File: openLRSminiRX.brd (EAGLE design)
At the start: 21.3 x 21.8 mm, 33 parts, among them IC1 MCP1703CB, U1 ATMEGA328P, Y1 16MHz

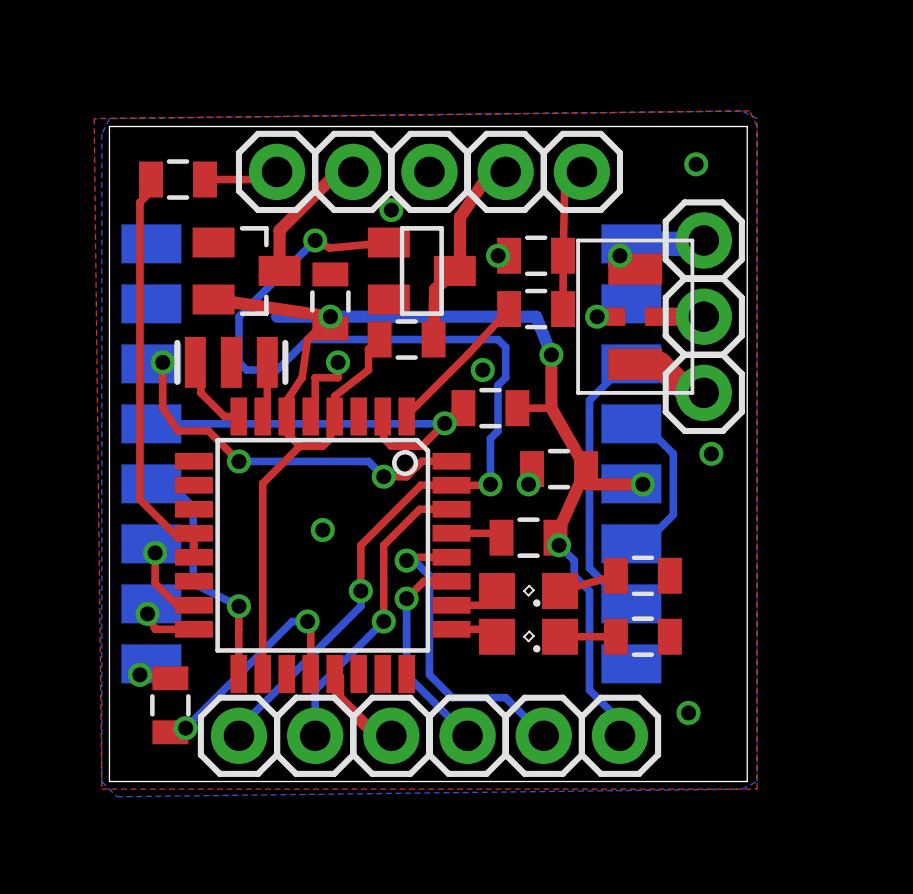
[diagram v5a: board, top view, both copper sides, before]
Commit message: Make filtter 'mandatory'. It is still possible to use without filter by soldering to pad directly.
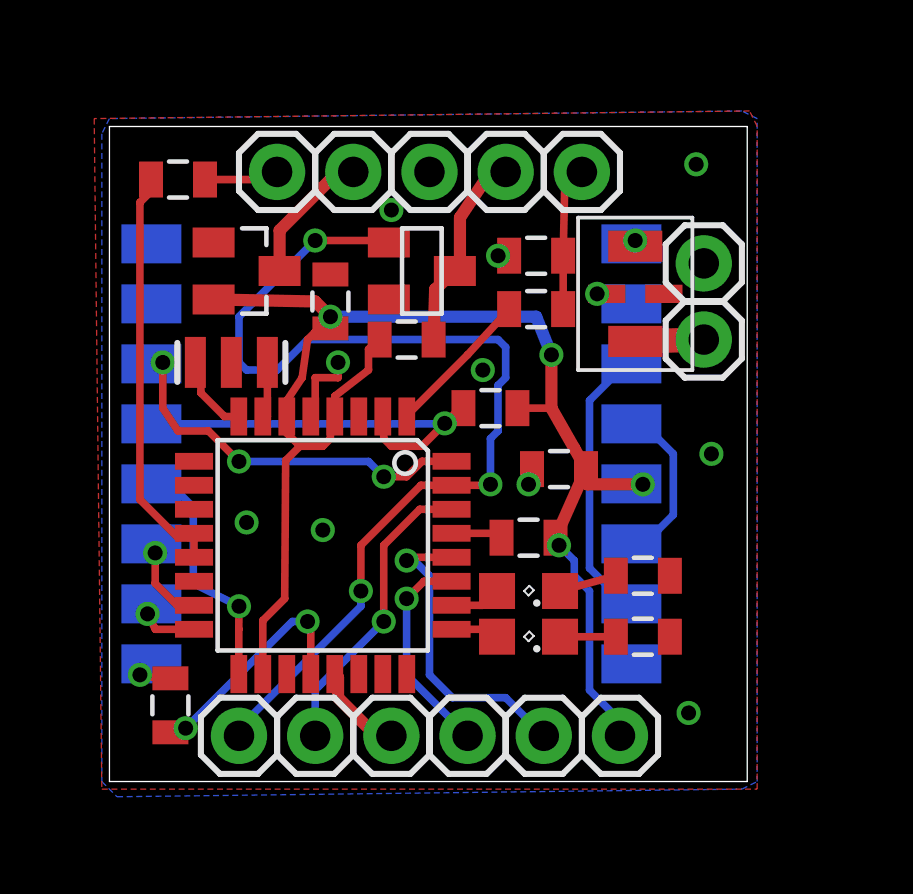
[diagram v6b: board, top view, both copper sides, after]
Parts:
- removed JP1: ANT, SparkFun-Connectors:1X01
- moved JP2 1.78 mm to (19.8, 14.7)
- moved JP8 1.78 mm to (19.8, 17.3)
- moved FILTER-1 0.76 mm to (17.5, 16.3)
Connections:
- net N$1: no longer JP1.1
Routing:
- net N$1: track 3.77 -> 0.36 mm
- net VCC: track 50.5 -> 48.8 mm
- net GND: vias 11 -> 12
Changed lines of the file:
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@@
 <?xml version="1.0" encoding="utf-8"?>
 <!DOCTYPE eagle SYSTEM "eagle.dtd">
-<eagle version="6.5.0">
+<eagle version="6.4">
 <drawing>
 <settings>
@@
 <attribute name="VALUE" x="15.24" y="18.923" size="0.4064" layer="27" rot="R180"/>
 </element>
-<element name="FILTER-1" library="minicircuits" package="FV1206" value="LFCN-490" x="17.526" y="15.494" smashed="yes" rot="R270"/>
-<element name="JP1" library="SparkFun-Connectors" package="1X01" value="ANT" x="19.812" y="18.034" smashed="yes"/>
-<element name="JP2" library="SparkFun-Connectors" package="1X01" value="ANTF" x="19.812" y="12.954" smashed="yes"/>
+<element name="FILTER-1" library="minicircuits" package="FV1206" value="LFCN-490" x="17.526" y="16.256" smashed="yes" rot="R270"/>
+<element name="JP2" library="SparkFun-Connectors" package="1X01" value="ANTF" x="19.812" y="14.732" smashed="yes"/>
 <element name="JP3" library="SparkFun-Connectors" package="1X01" value="RSSI" x="15.748" y="20.32" smashed="yes"/>
 <element name="JP5" library="SparkFun-Connectors" package="1X01" value="TXD" x="4.318" y="1.524" smashed="yes"/>
 <element name="JP6" library="SparkFun-Connectors" package="1X01" value="RXD" x="6.858" y="1.524" smashed="yes"/>
 <element name="JP7" library="SparkFun-Connectors" package="1X01" value="VIN" x="8.128" y="20.32" smashed="yes"/>
-<element name="JP8" library="SparkFun-Connectors" package="1X01" value="GND" x="19.812" y="15.494" smashed="yes"/>
+<element name="JP8" library="SparkFun-Connectors" package="1X01" value="GND" x="19.812" y="17.272" smashed="yes"/>
 <element name="JP9" library="SparkFun-Connectors" package="1X01" value="SDA" x="11.938" y="1.524" smashed="yes"/>
 <element name="JP10" library="SparkFun-Connectors" package="1X01" value="SCL" x="14.478" y="1.524" smashed="yes"/>
@@
 <via x="12.954" y="17.526" extent="1-16" drill="0.5"/>
 <via x="7.62" y="13.97" extent="1-16" drill="0.5"/>
-<via x="16.256" y="15.494" extent="1-16" drill="0.5"/>
+<via x="16.256" y="16.256" extent="1-16" drill="0.5"/>
 <via x="7.112" y="8.382" extent="1-16" drill="0.5"/>
 <via x="12.446" y="13.716" extent="1-16" drill="0.5"/>
@@
 <wire x1="6.858" y1="13.462" x2="7.62" y2="13.462" width="0.254" layer="1"/>
 <wire x1="7.62" y1="13.462" x2="7.62" y2="13.97" width="0.254" layer="1"/>
+<via x="4.572" y="8.636" extent="1-16" drill="0.5"/>
 </signal>
 <signal name="N$2">
@@
 <wire x1="7.366" y1="11.43" x2="7.366" y2="12.0206" width="0.254" layer="1"/>
 <wire x1="7.366" y1="12.0206" x2="7.512" y2="12.1666" width="0.254" layer="1"/>
-<wire x1="5.112" y1="3.5814" x2="5.112" y2="9.938" width="0.254" layer="1"/>
-<wire x1="5.112" y1="9.938" x2="6.35" y2="11.176" width="0.254" layer="1"/>
+<wire x1="5.112" y1="3.5814" x2="5.112" y2="5.366" width="0.254" layer="1"/>
+<wire x1="5.112" y1="5.366" x2="5.842" y2="6.096" width="0.254" layer="1"/>
+<wire x1="5.842" y1="6.096" x2="5.874" y2="10.7" width="0.254" layer="1"/>
+<wire x1="5.874" y1="10.7" x2="6.35" y2="11.176" width="0.254" layer="1"/>
 <wire x1="7.512" y1="12.1666" x2="7.512" y2="12.846" width="0.254" layer="1"/>
 <wire x1="7.512" y1="12.846" x2="8.636" y2="13.716" width="0.254" layer="1"/>
@@
 <wire x1="7.432" y1="15.428" x2="7.366" y2="15.494" width="0.254" layer="1"/>
 <via x="7.366" y="15.494" extent="1-16" drill="0.5"/>
-<wire x1="7.366" y1="15.494" x2="5.588" y2="15.494" width="0.4064" layer="16"/>
 <wire x1="7.366" y1="15.494" x2="14.224" y2="15.494" width="0.4064" layer="16"/>
 <wire x1="14.224" y1="15.494" x2="14.732" y2="14.224" width="0.4064" layer="16"/>
@@
 <wire x1="13.6" y1="12.446" x2="14.732" y2="12.446" width="0.254" layer="1"/>
 <wire x1="3.472" y1="16.068" x2="3.49" y2="16.068" width="0.4064" layer="1"/>
-<wire x1="3.49" y1="16.068" x2="7.366" y2="15.494" width="0.4064" layer="1"/>
+<wire x1="3.49" y1="16.068" x2="6.858" y2="16.002" width="0.4064" layer="1"/>
+<wire x1="6.858" y1="16.002" x2="7.366" y2="15.494" width="0.4064" layer="1"/>
 </signal>
 <signal name="N$7">
@@
 <wire x1="4.318" y1="15.494" x2="6.858" y2="18.034" width="0.254" layer="16"/>
 <via x="6.858" y="18.034" extent="1-16" drill="0.5"/>
-<wire x1="6.858" y1="18.034" x2="7.348" y2="17.78" width="0.254" layer="1"/>
-<wire x1="7.348" y1="17.78" x2="9.314" y2="17.968" width="0.254" layer="1"/>
+<wire x1="6.858" y1="18.034" x2="9.126" y2="18.034" width="0.254" layer="1"/>
+<wire x1="9.126" y1="18.034" x2="9.314" y2="17.968" width="0.254" layer="1"/>
 </signal>
 <signal name="PPM">
@@
 <contactref element="U$1" pad="1"/>
 <contactref element="FILTER-1" pad="1"/>
-<contactref element="JP1" pad="1"/>
-<wire x1="17.398" y1="17.922" x2="19.7" y2="17.922" width="0.8128" layer="16"/>
-<wire x1="19.7" y1="17.922" x2="19.812" y2="18.034" width="0.8128" layer="16"/>
-<wire x1="17.398" y1="17.922" x2="17.398" y2="17.906" width="0.8128" layer="16"/>
-<wire x1="17.398" y1="17.906" x2="17.018" y2="17.526" width="0.8128" layer="16"/>
-<via x="17.018" y="17.526" extent="1-16" drill="0.5"/>
-<wire x1="17.018" y1="17.526" x2="17.018" y2="17.3355" width="0.8128" layer="1"/>
-<wire x1="17.018" y1="17.3355" x2="17.526" y2="17.0815" width="0.8128" layer="1"/>
+<via x="17.526" y="18.034" extent="1-16" drill="0.5" diameter="0.254"/>
+<wire x1="17.526" y1="18.034" x2="17.526" y2="17.8435" width="0.4064" layer="1"/>
+<wire x1="17.398" y1="17.922" x2="17.526" y2="18.034" width="0.4064" layer="16"/>
 </signal>
 <signal name="N$4">
 <contactref element="FILTER-1" pad="3"/>
 <contactref element="JP2" pad="1"/>
-<wire x1="17.526" y1="13.9065" x2="18.3515" y2="13.9065" width="0.8128" layer="1"/>
-<wire x1="18.3515" y1="13.9065" x2="19.304" y2="12.954" width="0.8128" layer="1"/>
-<wire x1="19.304" y1="12.954" x2="19.812" y2="12.954" width="0.8128" layer="1"/>
+<wire x1="17.526" y1="14.6685" x2="19.812" y2="14.732" width="0.8128" layer="1"/>
 </signal>
 <signal name="VIN">

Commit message: Fix SBUS inverter (add resistor between TXD and NPN B) Add DTR breakout (easier serial flashing)
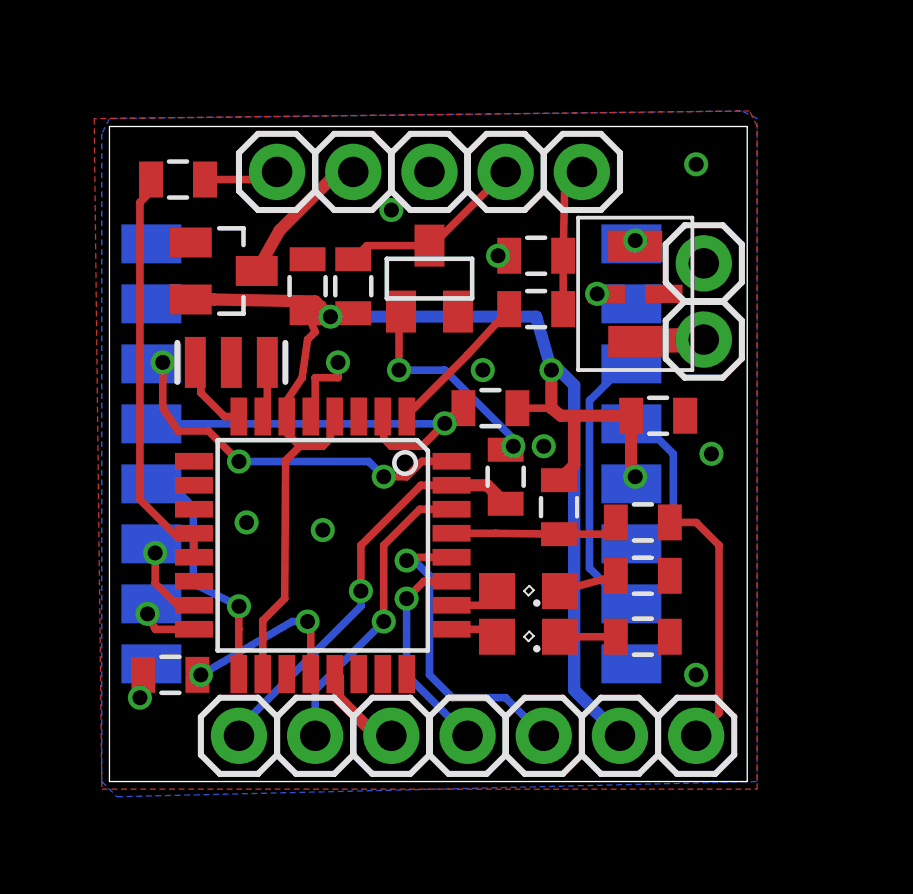
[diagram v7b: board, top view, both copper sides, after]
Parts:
- added C2: (no value), SparkFun-Capacitors:0805
- added JP1: DTR, SparkFun-Connectors:1X01
- added R8: (no value), SparkFun-Resistors:0805
- moved C5 3.75 mm to (18.3, 12.2), turned to 0 degrees
- moved R6 2.51 mm to (8.13, 16.5), turned to 270 degrees
- moved R5 1.44 mm to (15.0, 9.14), turned to 90 degrees
- moved C10 1.02 mm to (2.03, 3.56), turned to 0 degrees
- moved C6 0.92 mm to (6.60, 16.5)
- moved IC1 0.76 mm to (3.81, 17.0)
- moved Q1 0.36 mm to (10.7, 16.8), turned to 0 degrees
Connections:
- new net N$20: C2.1, JP1.1
- new net N$21: Q1.1, R8.1
- net N$18: now also C2.2
- net TXD: now also R8.2; no longer Q1.1
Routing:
- net TXD: track 35.1 -> 13.9 mm, vias 3 -> 1
- net N$20: track 0.00 -> 8.62 mm
- net N$21: track 0.00 -> 7.29 mm, vias 0 -> 2
- net VCC: track 48.8 -> 53.8 mm, vias 4 -> 3
- net N$18: track 1.71 -> 5.64 mm
- net N$19: track 7.89 -> 5.95 mm

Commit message: Add component values
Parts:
- C1, C6: value (none) -> 10uF
- C10, C2, C5: value (none) -> 100n
- LED1: value (none) -> green
- LED2: value (none) -> red
- Q1: value (none) -> mmbt2222
- R1, R2: value (none) -> 220R
- R3, R5, R8: value (none) -> 10k
- R4, R6, R7: value (none) -> 1k
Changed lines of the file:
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@@
 <?xml version="1.0" encoding="utf-8"?>
 <!DOCTYPE eagle SYSTEM "eagle.dtd">
-<eagle version="7.1.0">
+<eagle version="7.2.0">
 <drawing>
 <settings>
@@
 <attribute name="PROD_ID" value="IC-09069" x="7.112" y="7.874" size="1.778" layer="27" rot="R270" display="off"/>
 </element>
-<element name="R1" library="SparkFun-Resistors" package="0805" value="" x="17.78" y="4.826" smashed="yes">
+<element name="R1" library="SparkFun-Resistors" package="0805" value="220R" x="17.78" y="4.826" smashed="yes">
 <attribute name="VALUE" x="16.764" y="3.429" size="0.4064" layer="27"/>
 </element>
-<element name="LED1" library="led" package="SML0805" value="" x="13.97" y="4.826" smashed="yes" rot="R180">
+<element name="LED1" library="led" package="SML0805" value="green" x="13.97" y="4.826" smashed="yes" rot="R180">
 <attribute name="VALUE" x="15.47" y="6.826" size="1.27" layer="27" rot="R180"/>
 </element>
-<element name="LED2" library="led" package="SML0805" value="" x="13.97" y="6.35" smashed="yes" rot="R180">
+<element name="LED2" library="led" package="SML0805" value="red" x="13.97" y="6.35" smashed="yes" rot="R180">
 <attribute name="VALUE" x="15.47" y="8.35" size="1.27" layer="27" rot="R180"/>
 </element>
-<element name="R2" library="SparkFun-Resistors" package="0805" value="" x="17.78" y="6.858" smashed="yes">
+<element name="R2" library="SparkFun-Resistors" package="0805" value="220R" x="17.78" y="6.858" smashed="yes">
 <attribute name="VALUE" x="16.764" y="5.461" size="0.4064" layer="27"/>
 </element>
-<element name="R4" library="SparkFun-Resistors" package="0805" value="" x="14.224" y="15.748" smashed="yes" rot="R180">
+<element name="R4" library="SparkFun-Resistors" package="0805" value="1k" x="14.224" y="15.748" smashed="yes" rot="R180">
 <attribute name="VALUE" x="15.24" y="17.145" size="0.4064" layer="27" rot="R180"/>
 </element>
-<element name="C5" library="SparkFun-Capacitors" package="0805" value="" x="18.288" y="12.192" smashed="yes">
+<element name="C5" library="SparkFun-Capacitors" package="0805" value="100n" x="18.288" y="12.192" smashed="yes">
 <attribute name="VALUE" x="17.272" y="10.795" size="0.4064" layer="27"/>
 </element>
-<element name="C6" library="SparkFun-Capacitors" package="0805" value="" x="6.604" y="16.51" smashed="yes" rot="R90">
+<element name="C6" library="SparkFun-Capacitors" package="0805" value="10uF" x="6.604" y="16.51" smashed="yes" rot="R90">
 <attribute name="VALUE" x="8.001" y="15.494" size="0.4064" layer="27" rot="R90"/>
 </element>
-<element name="R5" library="SparkFun-Resistors" package="0805" value="" x="14.986" y="9.144" smashed="yes" rot="R90">
+<element name="R5" library="SparkFun-Resistors" package="0805" value="10k" x="14.986" y="9.144" smashed="yes" rot="R90">
 <attribute name="VALUE" x="16.383" y="8.128" size="0.4064" layer="27" rot="R90"/>
 </element>
-<element name="C10" library="SparkFun-Capacitors" package="0805" value="" x="2.032" y="3.556" smashed="yes">
+<element name="C10" library="SparkFun-Capacitors" package="0805" value="100n" x="2.032" y="3.556" smashed="yes">
 <attribute name="VALUE" x="1.016" y="2.159" size="0.4064" layer="27"/>
 </element>
-<element name="Q1" library="SparkFun-DiscreteSemi" package="SOT23" value="" x="10.668" y="16.764" smashed="yes">
+<element name="Q1" library="SparkFun-DiscreteSemi" package="SOT23" value="mmbt2222" x="10.668" y="16.764" smashed="yes">
 <attribute name="VALUE" x="9.652" y="16.5735" size="0.4064" layer="27"/>
 </element>
-<element name="R6" library="SparkFun-Resistors" package="0805" value="" x="8.128" y="16.51" smashed="yes" rot="R270">
+<element name="R6" library="SparkFun-Resistors" package="0805" value="1k" x="8.128" y="16.51" smashed="yes" rot="R270">
 <attribute name="VALUE" x="6.731" y="17.526" size="0.4064" layer="27" rot="R270"/>
 </element>
-<element name="C1" library="SparkFun-Capacitors" package="0805" value="" x="14.224" y="17.526" smashed="yes" rot="R180">
+<element name="C1" library="SparkFun-Capacitors" package="0805" value="10uF" x="14.224" y="17.526" smashed="yes" rot="R180">
 <attribute name="VALUE" x="15.24" y="18.923" size="0.4064" layer="27" rot="R180"/>
 </element>
@@
 <element name="JP13" library="SparkFun-Connectors" package="1X01" value="GND" x="9.398" y="1.524" smashed="yes"/>
 <element name="JP14" library="SparkFun-Connectors" package="1X01" value="GND" x="10.668" y="20.32" smashed="yes"/>
-<element name="R3" library="SparkFun-Resistors" package="0805" value="" x="12.7" y="12.446" smashed="yes" rot="R180">
+<element name="R3" library="SparkFun-Resistors" package="0805" value="10k" x="12.7" y="12.446" smashed="yes" rot="R180">
 <attribute name="VALUE" x="13.716" y="13.843" size="0.4064" layer="27" rot="R180"/>
 </element>
-<element name="R7" library="SparkFun-Resistors" package="0805" value="" x="2.286" y="20.066" smashed="yes" rot="R180">
+<element name="R7" library="SparkFun-Resistors" package="0805" value="1k" x="2.286" y="20.066" smashed="yes" rot="R180">
 <attribute name="VALUE" x="3.302" y="21.463" size="0.4064" layer="27" rot="R180"/>
 </element>
@@
 </element>
 <element name="JP1" library="SparkFun-Connectors" package="1X01" value="DTR" x="19.558" y="1.524" smashed="yes"/>
-<element name="C2" library="SparkFun-Capacitors" package="0805" value="" x="17.78" y="8.636" smashed="yes" rot="R180">
+<element name="C2" library="SparkFun-Capacitors" package="0805" value="100n" x="17.78" y="8.636" smashed="yes" rot="R180">
 <attribute name="VALUE" x="18.796" y="10.033" size="0.4064" layer="27" rot="R180"/>
 </element>
-<element name="R8" library="SparkFun-Resistors" package="0805" value="" x="13.208" y="10.16" smashed="yes" rot="R270">
+<element name="R8" library="SparkFun-Resistors" package="0805" value="10k" x="13.208" y="10.16" smashed="yes" rot="R270">
 <attribute name="VALUE" x="11.811" y="11.176" size="0.4064" layer="27" rot="R270"/>
 </element>
